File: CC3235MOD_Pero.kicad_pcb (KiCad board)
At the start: 2 copper layers, 57.9 x 34.3 mm, 38 parts, among them J1 USB_B_Mini, J2 JTAG/SWD, SW1 Reset, SW2 SW_DIP_x03, SW3 User IO, U1 TLV1117-33, U2 CP2102N-A01-GQFN24, U3 CC3235MODSF12MOBR

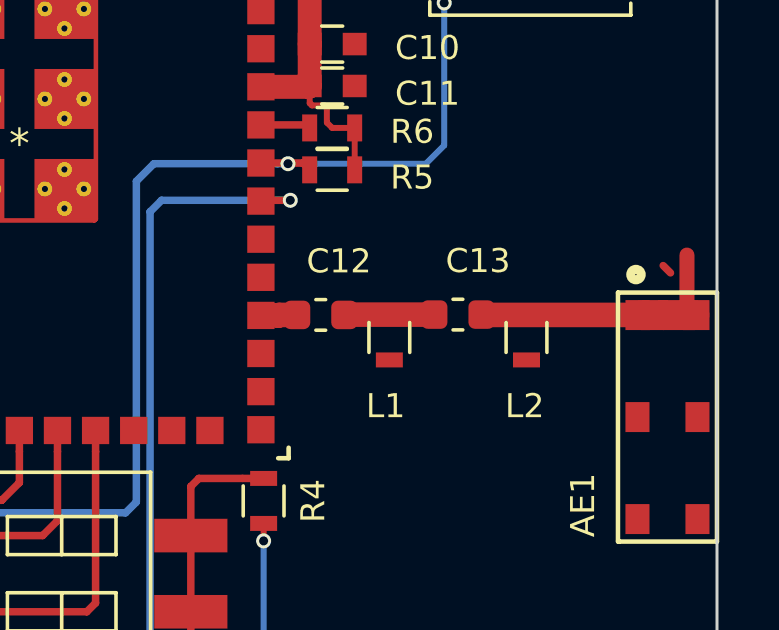
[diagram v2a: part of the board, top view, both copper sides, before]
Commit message: 50Ohm trace adapted for 1.6mm PCB
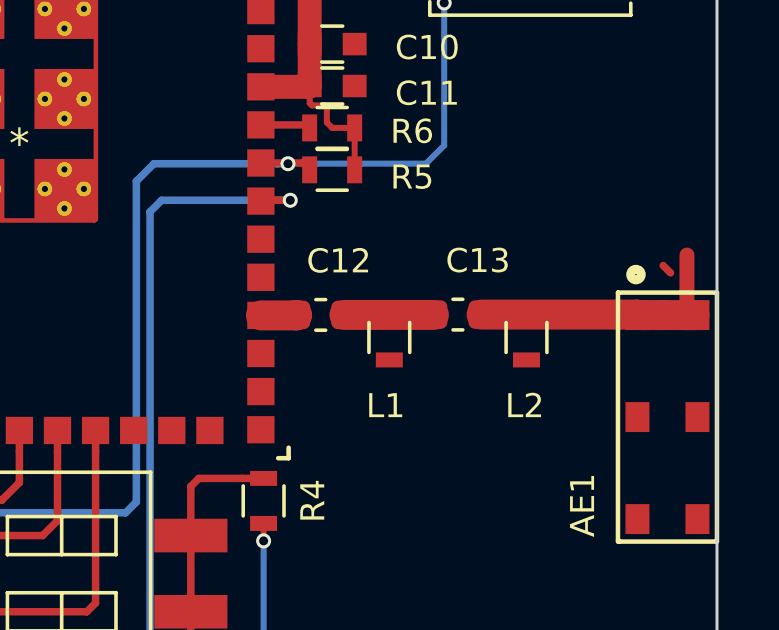
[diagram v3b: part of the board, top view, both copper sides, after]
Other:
- net class RF: trace_width 0.82 -> 1.08
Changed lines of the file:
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@@
   (layers
     (0 F.Cu signal)
-    (31 B.Cu signal)
+    (31 B.Cu signal hide)
     (32 B.Adhes user hide)
     (33 F.Adhes user)
@@
   )
   (setup
-    (last_trace_width 0.5)
+    (last_trace_width 1)
     (user_trace_width 0.2)
     (user_trace_width 0.25)
@@
     (edge_width 0.15)
     (segment_width 0.2)
-    (pcb_text_width 0.3)
+    (pcb_text_width 0.2)
     (pcb_text_size 0.8 1)
     (mod_edge_width 0.15)
@@
   (net_class RF ""
     (clearance 0.2)
-    (trace_width 0.82)
+    (trace_width 1.08)
     (via_dia 0.8)
     (via_drill 0.3)
@@
   (segment (start 165.976203 112.263203) (end 165.976203 111.558203) (width 0.25) (layer F.Cu) (net 7) (status 20))
   (segment (start 165.6842 117.602) (end 165.976203 117.309997) (width 0.25) (layer F.Cu) (net 7))
-  (segment (start 171.486202 107.723202) (end 172.076798 107.723202) (width 0.82) (layer F.Cu) (net 8) (status 10))
-  (segment (start 172.093 107.707) (end 172.5975 107.707) (width 0.82) (layer F.Cu) (net 8) (status 20))
-  (segment (start 172.076798 107.723202) (end 172.093 107.707) (width 0.82) (layer F.Cu) (net 8))
   (segment (start 160.541 120.142) (end 161.201 120.142) (width 0.25) (layer F.Cu) (net 9) (status 30))
   (via (at 162.3822 120.142) (size 0.5) (drill 0.3) (layers F.Cu B.Cu) (net 9))
@@
   (segment (start 178.8415 107.696) (end 178.8525 107.707) (width 0.82) (layer F.Cu) (net 1))
   (segment (start 184.18356 107.707) (end 184.18886 107.7123) (width 0.82) (layer F.Cu) (net 1))
-  (segment (start 178.8525 107.707) (end 184.18356 107.707) (width 0.82) (layer F.Cu) (net 1))
   (segment (start 184.8957 107.7123) (end 185.58886 107.7123) (width 1) (layer F.Cu) (net 1))
   (segment (start 184.18886 107.7123) (end 184.8957 107.7123) (width 1) (layer F.Cu) (net 1))
@@
   (segment (start 184.8957 107.7123) (end 185.1406 107.4674) (width 0.25) (layer F.Cu) (net 1))
   (segment (start 185.68886 107.7123) (end 185.68886 105.71114) (width 0.5) (layer F.Cu) (net 1))
-  (segment (start 174.359 107.696) (end 177.2665 107.696) (width 0.82) (layer F.Cu) (net 30))
+  (segment (start 184.02256 107.696) (end 184.03886 107.7123) (width 1) (layer F.Cu) (net 1))
+  (segment (start 178.8415 107.696) (end 184.02256 107.696) (width 1) (layer F.Cu) (net 1))
+  (segment (start 171.486202 107.723202) (end 172.678298 107.723202) (width 1) (layer F.Cu) (net 8))
+  (segment (start 172.678298 107.723202) (end 172.6945 107.707) (width 1) (layer F.Cu) (net 8))
+  (segment (start 174.2695 107.707) (end 177.2555 107.707) (width 1) (layer F.Cu) (net 30))
   (zone (net 29) (net_name VBUS) (layer F.Cu) (hatch edge 0.508)
     (priority 2)
@@
     (polygon
       (pts
-        (xy 172.8724 107.1118) (xy 182.6514 107.1118) (xy 182.626 108.3056) (xy 172.847 108.3056)
+        (xy 172.21 107) (xy 182.6 107) (xy 182.6 108.4) (xy 172.21 108.4)
       )
     )

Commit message: via stitching
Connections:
- U3 pad V: (no net) -> GND
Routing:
- net GND: vias 16 -> 126
- net (no net): vias 0 -> 7

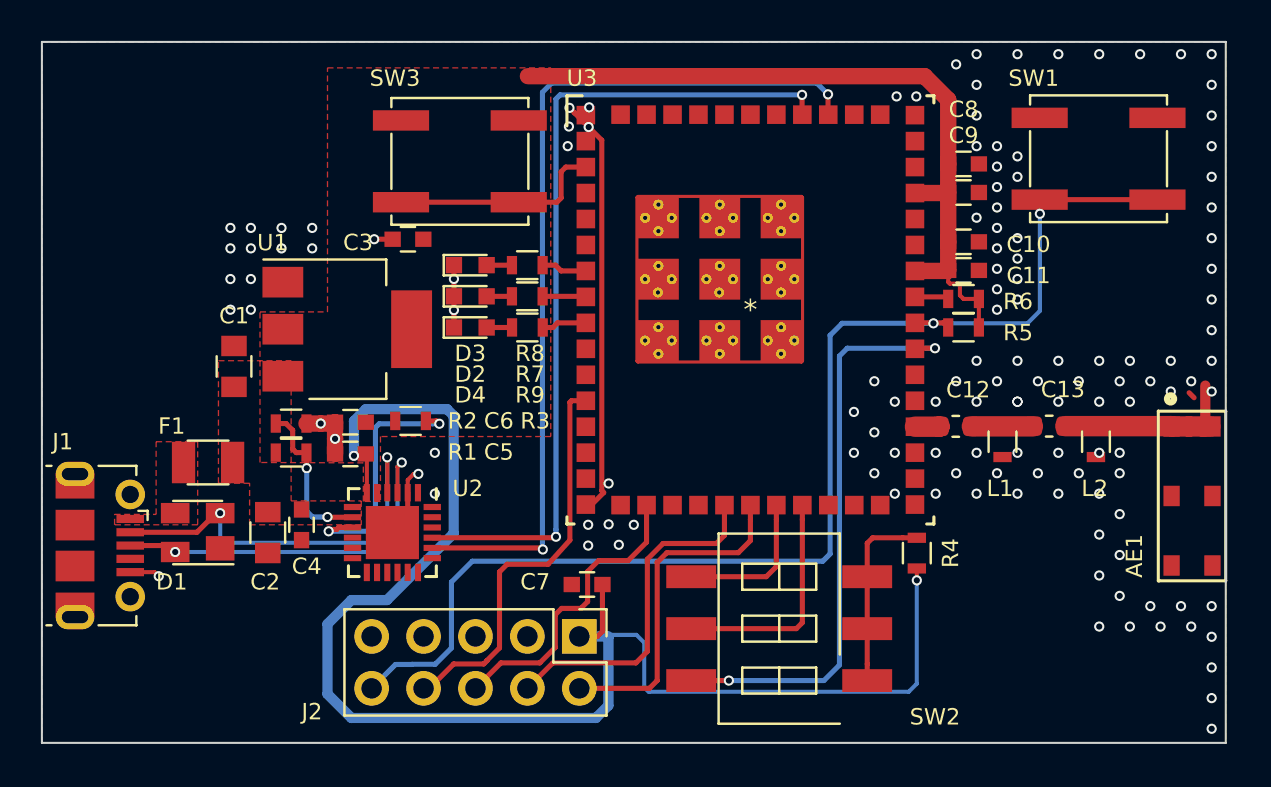
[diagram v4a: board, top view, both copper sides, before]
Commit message: silkscreen finished, ready to order
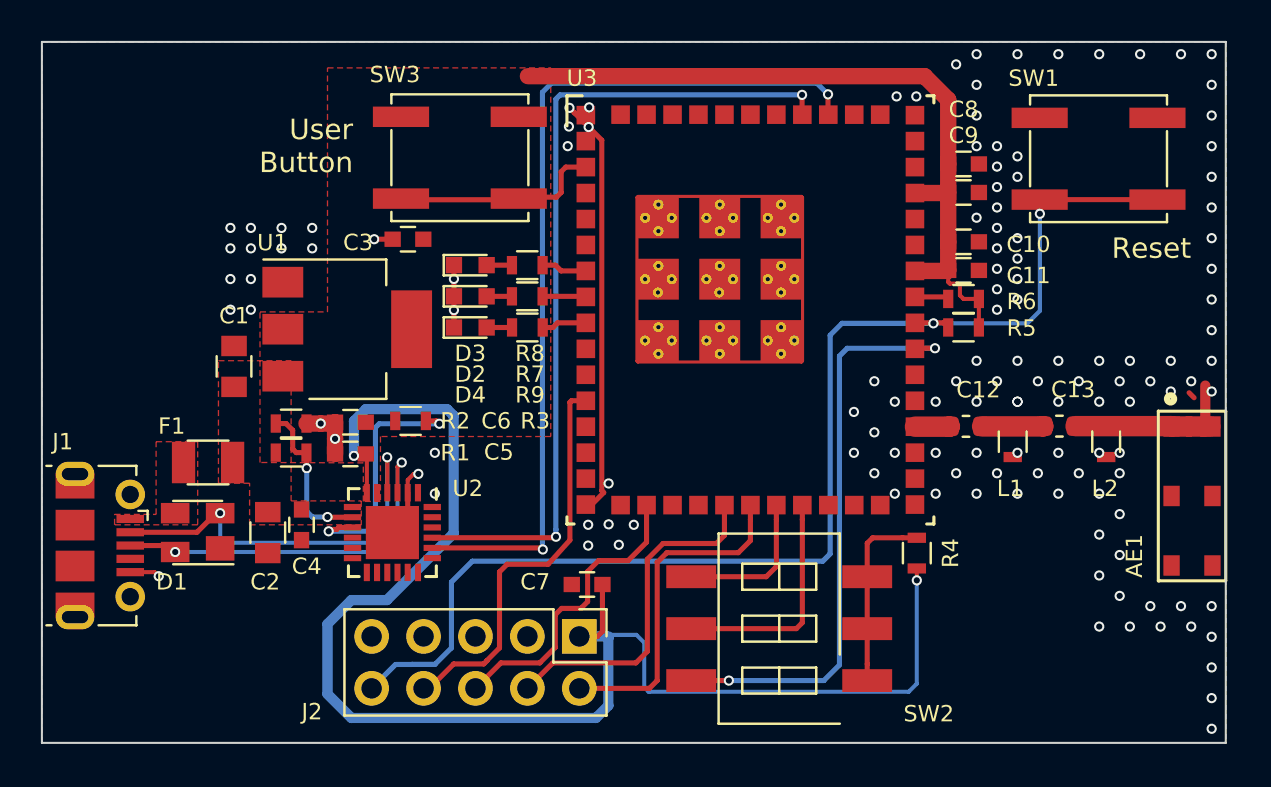
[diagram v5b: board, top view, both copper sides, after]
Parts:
- moved C12 0.50 mm to (174.0, 107.7)
- moved C13 0.50 mm to (178.6, 107.7)
- moved L1 0.50 mm to (176.3, 108.5)
- moved L2 0.50 mm to (180.8, 108.5)
- moved SW3 0.18 mm to (149.2, 94.6)
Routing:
- net GND: track 41.3 -> 40.8 mm
- net /RF_OUT: track 1.22 -> 1.72 mm
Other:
- board text added: "Boot config: 100 Flash programming 000 Functional mode and 4-wireJTAG 001 Functional mode and SWD 010 Functional mode and flash"
- board text added: "CC3235MOD Test Board"
- board text added: "Pero, 2020"
- board text added: "Reset"
- board text added: "Rev A0"
- board text added: "User Button"
- board text added: "www.helentronica.com"

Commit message: adding a hash number
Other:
- board text added: "Rev A0 (21e8d16)"
- board text removed: "Rev A0"
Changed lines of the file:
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@@
     (effects (font (size 1 1) (thickness 0.2)) (justify left mirror))
   )
-  (gr_text "Rev A0" (at 180 117) (layer B.SilkS)
+  (gr_text "Rev A0 (21e8d16)" (at 171.4246 117.0432) (layer B.SilkS)
     (effects (font (size 1 1) (thickness 0.2)) (justify right mirror))
   )

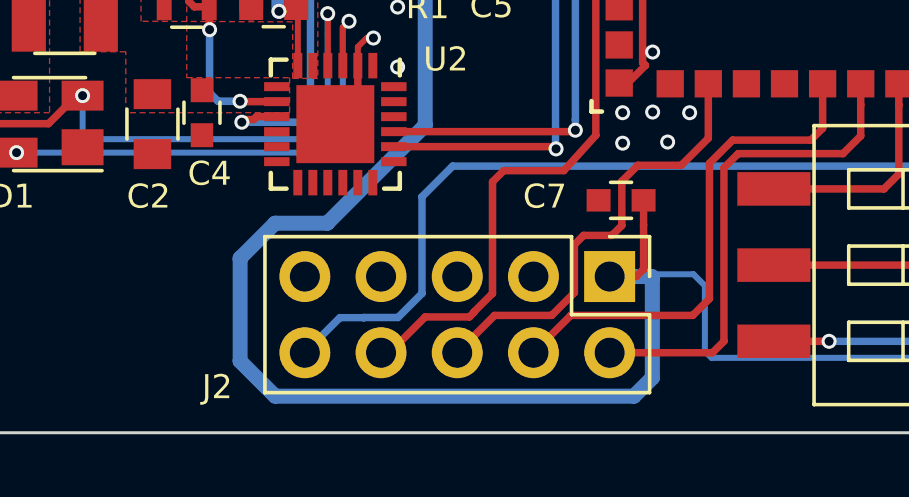
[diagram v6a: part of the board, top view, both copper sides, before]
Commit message: SWD silkscreen
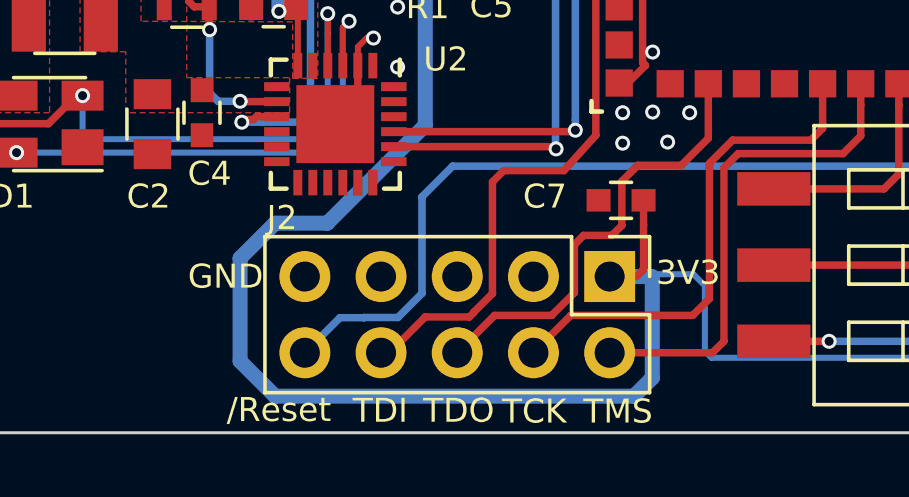
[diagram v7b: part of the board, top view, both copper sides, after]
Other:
- board text added: "/Reset"
- board text added: "3V3"
- board text added: "GND"
- board text added: "TCK"
- board text added: "TDI"
- board text added: "TDO"
- board text added: "TMS"
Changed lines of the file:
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@@
   (general
     (thickness 1.6)
-    (drawings 14)
+    (drawings 21)
     (tracks 406)
     (zones 0)
@@
   (page A4)
   (layers
-    (0 F.Cu signal hide)
+    (0 F.Cu signal)
     (31 B.Cu signal hide)
     (32 B.Adhes user hide)
@@
     (pad_to_mask_clearance 0.2)
     (aux_axis_origin 0 0)
-    (visible_elements 7FFFFFFF)
+    (visible_elements 7FFDFFFF)
     (pcbplotparams
       (layerselection 0x010fc_ffffffff)
@@
     (descr "Through hole straight pin header, 2x05, 2.54mm pitch, double rows")
     (tags "Through hole pin header THT 2x05 2.54mm double row")
-    (fp_text reference J2 (at 3.683 13.081 180) (layer F.SilkS)
+    (fp_text reference J2 (at -1.9558 10.922 180) (layer F.SilkS)
       (effects (font (size 0.8 0.8) (thickness 0.15)))
     )
@@
       (net 1 GND))
   )
+  (gr_text GND (at 142.2654 117.983) (layer F.SilkS)
+    (effects (font (size 0.8 0.8) (thickness 0.15)))
+  )
+  (gr_text 3V3 (at 157.6832 117.856) (layer F.SilkS)
+    (effects (font (size 0.8 0.8) (thickness 0.15)))
+  )
+  (gr_text /Reset (at 144.0434 122.428) (layer F.SilkS)
+    (effects (font (size 0.8 0.8) (thickness 0.15)))
+  )
+  (gr_text TDI (at 147.4216 122.4534) (layer F.SilkS)
+    (effects (font (size 0.8 0.8) (thickness 0.15)))
+  )
+  (gr_text TDO (at 150.0378 122.4534) (layer F.SilkS)
+    (effects (font (size 0.8 0.8) (thickness 0.15)))
+  )
+  (gr_text TCK (at 152.5524 122.4788) (layer F.SilkS)
+    (effects (font (size 0.8 0.8) (thickness 0.15)))
+  )
+  (gr_text TMS (at 155.3464 122.4788) (layer F.SilkS)
+    (effects (font (size 0.8 0.8) (thickness 0.15)))
+  )
   (gr_text "Boot config:\n100   Flash programming\n000   Functional mode and 4-wireJTAG\n001   Functional mode and SWD\n010   Functional mode and flash" (at 138.6332 122.3772 270) (layer B.SilkS)
